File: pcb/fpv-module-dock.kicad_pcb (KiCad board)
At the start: 2 copper layers, 80 x 50 mm, 12 parts, among them J1 Barrel_Jack_Switch, J2 AudioJack4_SwitchTR1, J3 Conn_01x09, SW1 SW_SPDT, SW2 SW_Push, SW3 SW_Push, SW4 SW_Push, U1 2850

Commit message: Working on layout
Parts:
- moved J3 26.0 mm to (156.0, 91.3)
- moved H2 24.4 mm to (163.0, 87.0)
- moved H3 23.0 mm to (163.0, 121.0)
- moved U1 9.85 mm to (132.0, 105.0)
- moved H1 8.00 mm to (114.0, 87.0)
- moved SW1 7.59 mm to (122.6, 85.2)
- moved SW2 7.49 mm to (164.8, 91.8), turned to 270 degrees
- moved J2 5.00 mm to (111.0, 98.0)
- moved SW3 4.26 mm to (164.8, 100.8), turned to 270 degrees
- moved J1 4.00 mm to (110.0, 112.0)
- moved SW4 3.48 mm to (164.8, 109.8), turned to 270 degrees
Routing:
- added copper zone on B.Cu, net GND
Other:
- board size 80 x 50 mm -> 57 x 42 mm

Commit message: Added 3D models, completed layout
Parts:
- H1, H2, H3, H4: footprint MountingHole:MountingHole_3.2mm_M3_Pad -> MountingHole:MountingHole_3.2mm_M3
- J1, J2, U1: moved to B.Cu
- J3: moved to F.Cu
- SW1: footprint Button_Switch_THT:SW_Slide_1P2T_CK_OS102011MS2Q -> fpv-module-dock:OS102011MA1QN1; moved to B.Cu
- SW2, SW3, SW4: footprint Button_Switch_THT:SW_PUSH_6mm_H13mm -> Button_Switch_THT:SW_Tactile_SPST_Angled_PTS645Vx83-2LFS; moved to B.Cu
- moved SW1 45.1 mm to (164.8, 101.0), turned to 90 degrees
- moved SW4 42.9 mm to (129.0, 86.0), turned to 180 degrees
- moved SW3 28.0 mm to (141.0, 86.0), turned to 180 degrees
- moved U1 18.4 mm to (150.0, 109.0), turned to 180 degrees
- moved SW2 13.1 mm to (153.0, 86.0), turned to 180 degrees
- moved J3 4.25 mm to (156.0, 95.6), turned to 0 degrees
- moved J1 3.00 mm to (110.0, 109.0)
- moved J2 1.00 mm to (111.0, 97.0)
- moved H1 0.71 mm to (113.5, 86.5)
- moved H2 0.71 mm to (163.5, 86.5)
- moved H3 0.71 mm to (163.5, 121.5)
- moved H4 0.71 mm to (113.5, 121.5)
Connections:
- SW1 pad 1: Net-(SW1-Pad1) -> GND
- SW1 pad 3: GND -> Net-(SW1-Pad3)
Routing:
- net /VIDEO: track 0.00 -> 47.6 mm
- net Net-(SW1-Pad2): track 0.00 -> 47.4 mm
- net /AUDIO_R: track 0.00 -> 43.7 mm
- net /AUDIO_L: track 0.00 -> 41.2 mm
- net Net-(J3-Pad3): track 0.00 -> 38.5 mm
- net +5V: track 0.00 -> 34.7 mm
- net Net-(J3-Pad2): track 0.00 -> 28.9 mm
- net +BATT: track 0.00 -> 22.9 mm
- net Net-(J3-Pad1): track 0.00 -> 14.7 mm
- net GND: track 0.00 -> 2.34 mm, vias 0 -> 1
- added copper zone on B.Cu, net (none)
- added copper zone on F.Cu, net GND
- removed copper zone on B.Cu, net GND
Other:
- outline, holes or cut-outs redrawn
- net class Default: clearance 0.2 -> 0.1524; trace_width 0.25 -> 0.1524; via_dia 0.8 -> 0.6858; via_drill 0.4 -> 0.3302
- net class Power added: clearance 0.1524, trace_width 0.762, via_dia 0.6858, via_drill 0.3302
- rule pad_to_mask_clearance: 0 -> 0.000051
- rule trace_clearance: 0.2 -> 0.1524
- rule trace_min: 0.2 -> 0.1524
- rule via_min_drill: 0.3 -> 0.254
- rule via_min_size: 0.4 -> 0.508
- board text added: "FPV Module Docking Station"

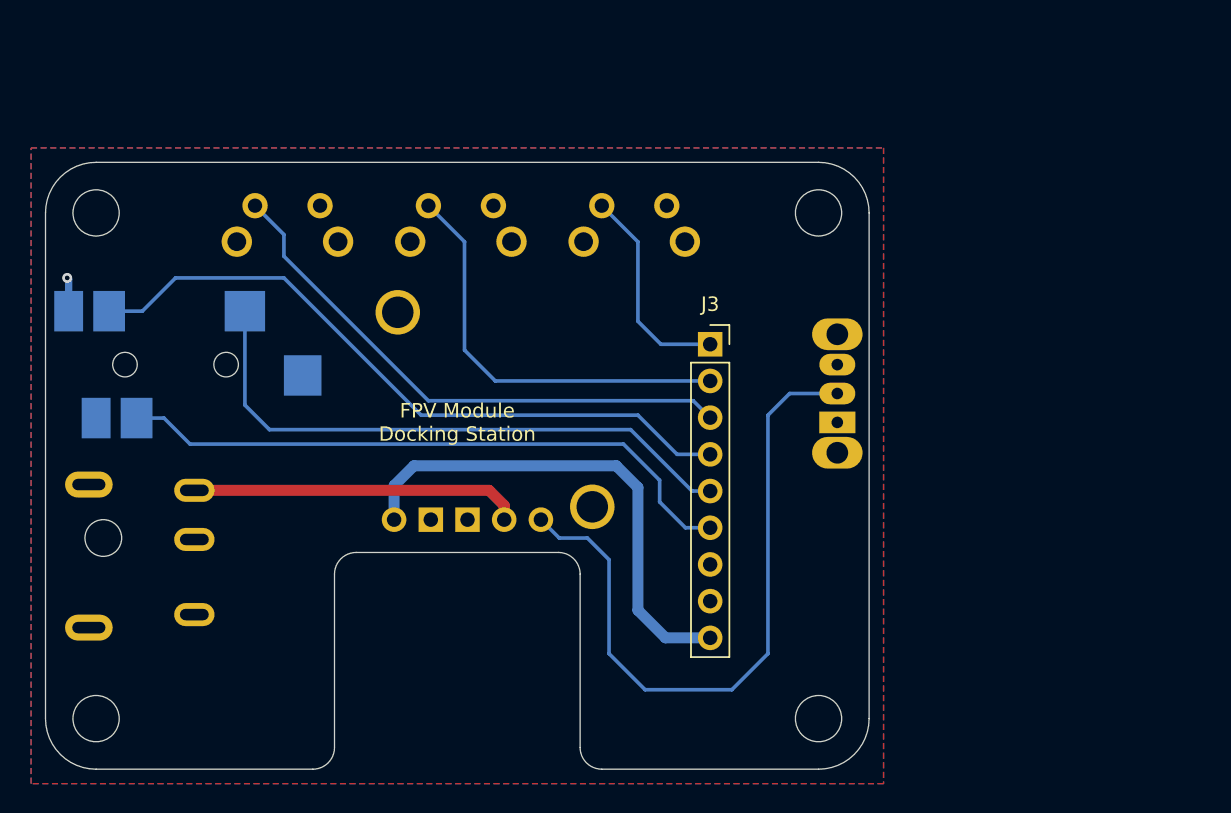
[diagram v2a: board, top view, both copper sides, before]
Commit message: Added power LED
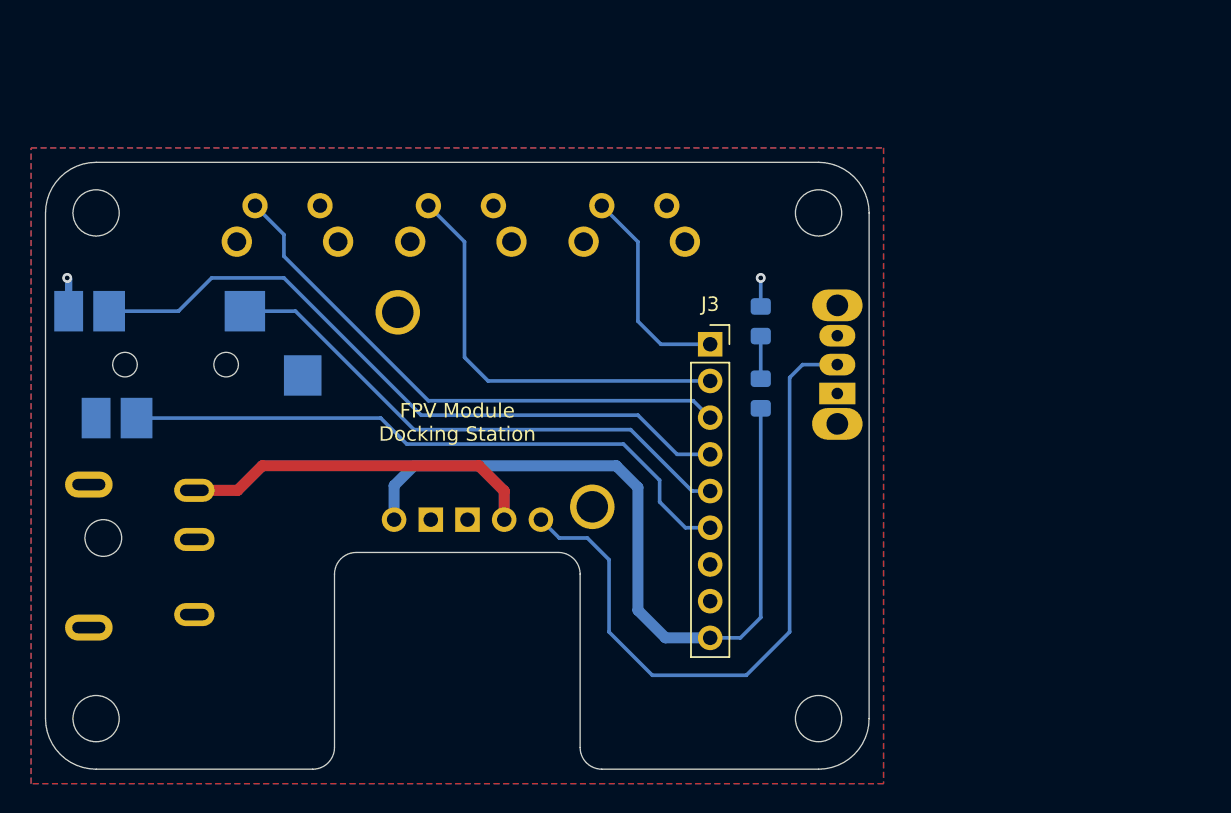
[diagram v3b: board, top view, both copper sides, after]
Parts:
- added D1: LED, LED_SMD:LED_0805_2012Metric_Pad1.15x1.40mm_HandSolder, B.Cu at (159.5, 94.0)
- added R1: 1k, Resistor_SMD:R_0805_2012Metric_Pad1.15x1.40mm_HandSolder, B.Cu at (159.5, 99.0)
- moved SW1 2.00 mm to (164.8, 99.0)
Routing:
- net +5V: track 34.7 -> 53.3 mm
- net /AUDIO_L: track 41.2 -> 37.4 mm
- net Net-(D1-Pad2): track 0.00 -> 2.95 mm
- net +BATT: track 22.9 -> 24.9 mm
- net GND: track 2.34 -> 4.32 mm, vias 1 -> 2
